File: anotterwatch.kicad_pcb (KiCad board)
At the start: 4 copper layers, 48.5 x 43 mm, 132 parts, among them J1 Micro_SD_Card, J2 Shitty Add-On, J3 Conn_01x05, J4 USB_C_Receptacle_USB2.0, Q1 AO3400, Q2 AO3400, Q3 AO3400, Q4 AO3400, Q5 AO3400, Q6 AO3400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

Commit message: Finished layout
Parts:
- removed C24: 100p, Capacitor_SMD:C_0402_1005Metric
- removed R47: 390k, Resistor_SMD:R_0402_1005Metric
- added C37: 470p, Capacitor_SMD:C_0402_1005Metric, B.Cu at (92.2, 75.7)
- added R50: 10, Resistor_SMD:R_0603_1608Metric, B.Cu at (105.3, 89.5)
- LS1: footprint Connector_Molex:Molex_KK-254_AE-6410-02A_1x02_P2.54mm_Vertical -> Resistor_SMD:R_2816_7142Metric; moved to B.Cu
- moved Q6 85.7 mm to (93.9, 87.8)
- moved LS1 76.6 mm to (100.3, 85.9), turned to 220 degrees
- moved C9 46.9 mm to (87.2, 83.3), turned to 90 degrees
- moved C10 41.2 mm to (91.9, 87.8), turned to 90 degrees
- moved C29 34.6 mm to (96.8, 99.2), turned to 270 degrees
- moved C15 34.1 mm to (104.1, 87.5), turned to 90 degrees
- moved R24 34.0 mm to (103.0, 87.9), turned to 270 degrees
- moved D3 31.2 mm to (86.5, 109.0)
- moved D4 31.2 mm to (118.0, 109.0)
- moved C26 27.3 mm to (80.2, 81.4)
- moved C11 20.2 mm to (112.1, 92.0), turned to 90 degrees
- moved C16 16.7 mm to (114.7, 107.3), turned to 180 degrees
- moved C3 14.5 mm to (89.1, 78.9), turned to 90 degrees
- moved C4 8.43 mm to (106.0, 76.8)
- moved R18 7.41 mm to (106.5, 85.5)
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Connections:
- D5 pad K: (no net) -> +BATT
- J2 pad 1: I2C_SDA -> +3V3
- J2 pad 2: +3V3 -> I2C_SDA
- J2 pad 3: I2C_SCL -> GND
- J2 pad 4: GND -> I2C_SCL
- J4 pad S1: Net-(C24-Pad2) -> GND
- SW1 pad : (no net) -> GND
- U1 pad 12: (no net) -> GND
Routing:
- net Net-(C31-Pad1): track 0.00 -> 116.9 mm, vias 0 -> 5
- net I2C_SDA: track 3.64 -> 76.1 mm, vias 0 -> 6
- net I2C_SCL: track 4.53 -> 67.9 mm, vias 0 -> 5
- net VBUS: track 7.18 -> 58.5 mm, vias 0 -> 8
- net +3V3: track 25.8 -> 70.3 mm, vias 2 -> 27
- net Net-(D2-Pad1): track 0.00 -> 42.0 mm, vias 0 -> 2
- net Net-(D1-Pad1): track 0.00 -> 37.9 mm, vias 0 -> 2
- net BTN_DOWN: track 0.00 -> 34.7 mm, vias 0 -> 3
- net BTN_UP: track 4.80 -> 38.5 mm, vias 0 -> 2
- net BTN_CNTR: track 0.00 -> 33.5 mm, vias 0 -> 3
- net ADC_REF: track 8.34 -> 41.3 mm, vias 0 -> 2
- net Net-(D3-Pad1): track 0.00 -> 31.7 mm, vias 0 -> 2
- net IO0: track 9.60 -> 38.8 mm
- net TXD: track 0.00 -> 28.2 mm, vias 0 -> 2
- net RXD: track 0.00 -> 28.1 mm, vias 0 -> 2
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- added copper zone on In2.Cu, net +3V3
- added copper zone on F.Cu, net GND
- added copper zone on In2.Cu, net GNDA
- removed copper zone on B.Cu, net VBUS

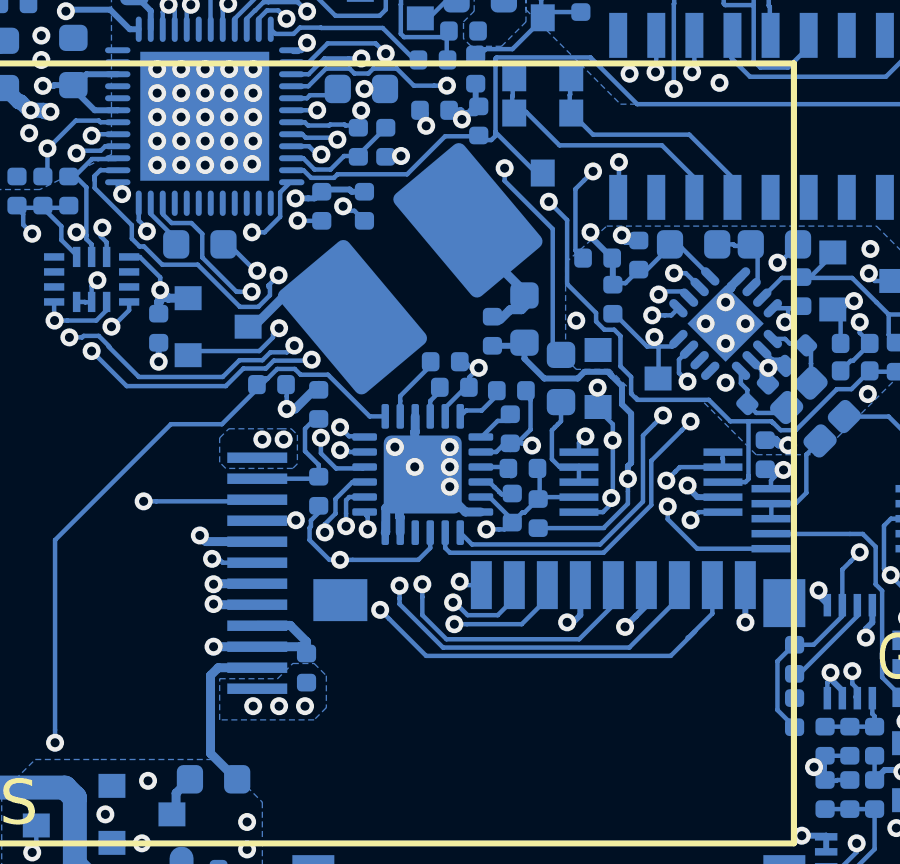
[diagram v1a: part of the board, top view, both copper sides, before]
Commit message: Finished silkscreen
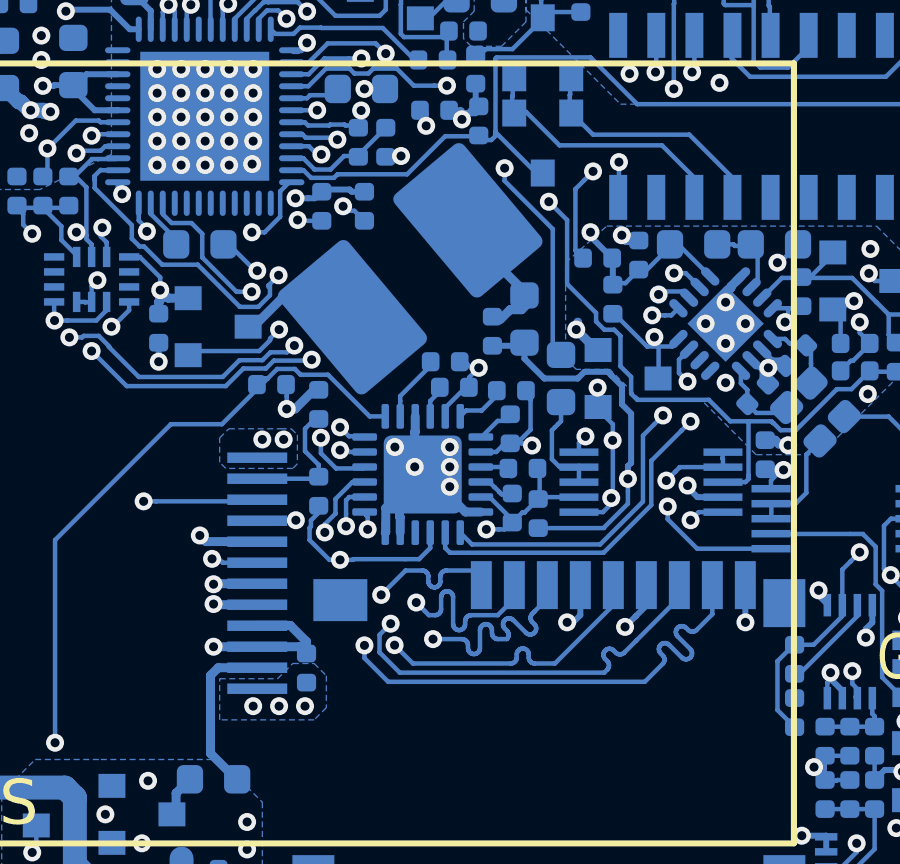
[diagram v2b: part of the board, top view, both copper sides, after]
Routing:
- net ADC_SCK: track 27.9 -> 33.2 mm
- net SD_DATA2: track 31.0 -> 36.1 mm
- net SD_CMD: track 32.1 -> 36.9 mm
- net SD_DATA3: track 32.8 -> 37.5 mm
- net ADC_MISO: track 24.4 -> 29.0 mm
- net SD_DATA1: track 32.4 -> 35.5 mm
- net Net-(J1-Pad7): track 34.0 -> 36.0 mm
- net GND: track 53.2 -> 54.4 mm
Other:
- board text added: "SPEAKER"

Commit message: Final design for first prototype
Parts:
- moved R8 0.05 mm to (97.3, 83.8)
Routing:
- net Net-(AE1-Pad1): track 2.43 -> 4.97 mm
- net Net-(C6-Pad1): track 2.54 -> 4.10 mm
- net GND: vias 129 -> 127

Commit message: ADD: finalized artwork, first pcbs ordered
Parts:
- added G***: LOGO, badgelib:AnOtterWatch_SilkScreen, F.Cu at (103.3, 90.1)
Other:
- board text removed: "-"
- board text removed: "A B GND C CH1 CH2"
- board text removed: "IPS"
- board text removed: "Scope 60V!"
- board text removed: "Tester 3.3V!"

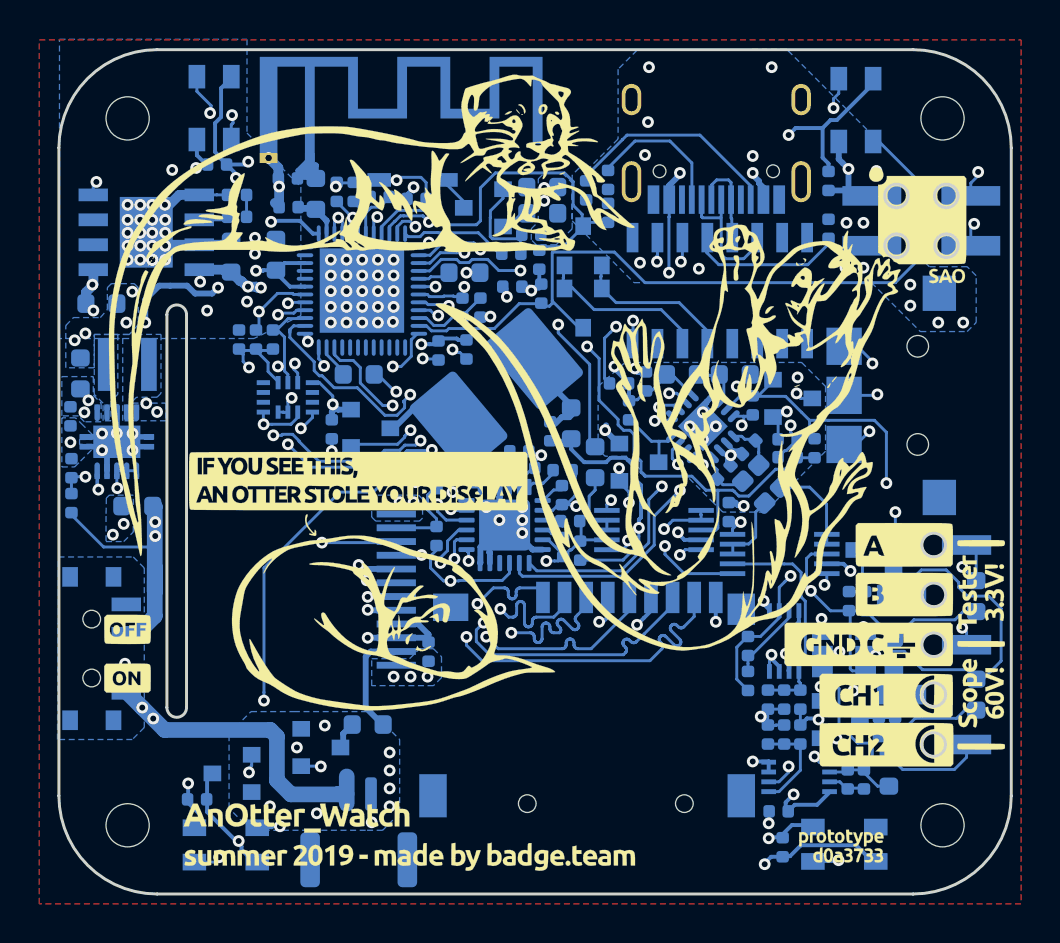
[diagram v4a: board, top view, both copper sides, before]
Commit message: FIX: ESP32 new footprint, fix LED polarity, fix IPS FFC position
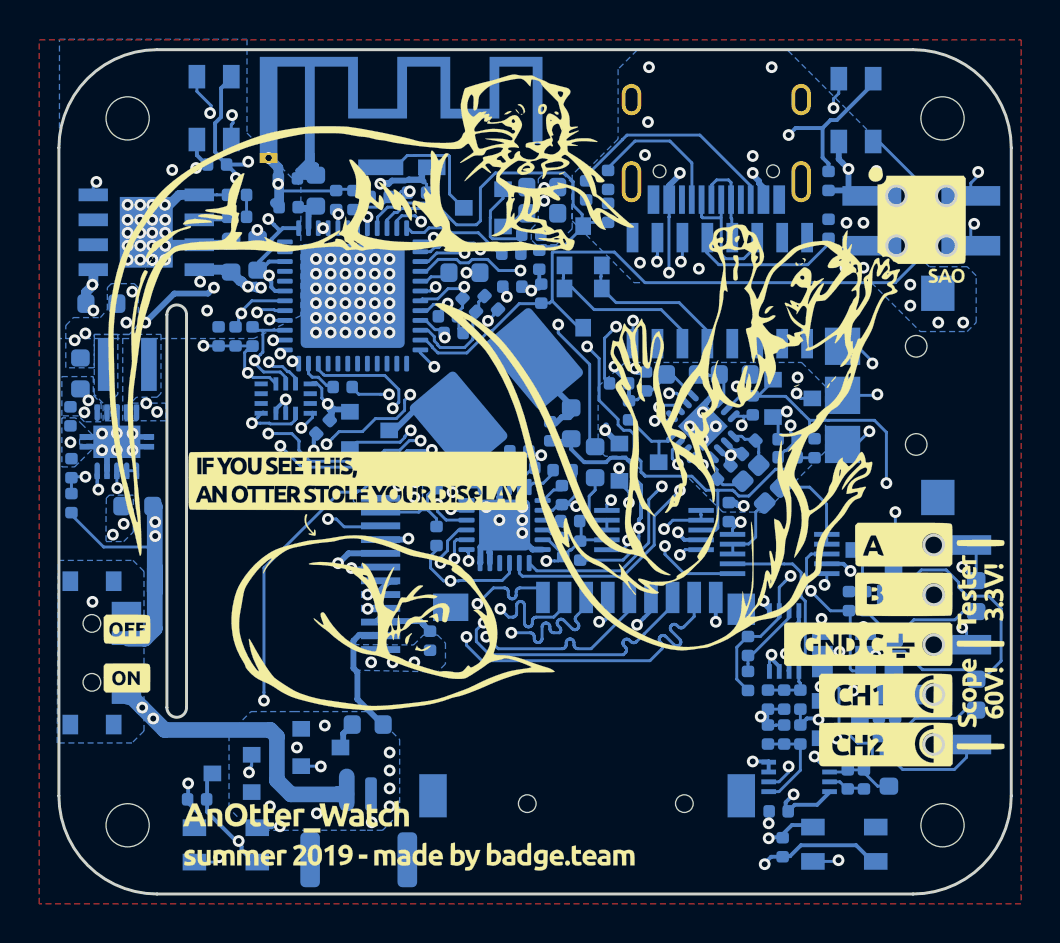
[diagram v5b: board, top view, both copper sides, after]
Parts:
- BT1: footprint badgelib:JST_GH_BM02B-GHS-TBT_1x02-1MP_P1.25mm_Vertical -> Connector_JST:JST_GH_BM02B-GHS-TBT_1x02-1MP_P1.25mm_Vertical
- C6: value TBD -> 4p7
- C7: value TBD -> 3p9
- D5: footprint badgelib:RZX-S020CCW-0.4T -> badgelib:A150GKCBBUP5A
- J1: footprint badgelib:SUNTECH_ST-TF-003A -> ST-TF-003A:SUNTECH_ST-TF-003A
- L1: value TBD -> 1n8
- R13: footprint Resistor_SMD:R_0603_1608Metric -> Resistor_SMD:R_0402_1005Metric
- R16: value 5k1 -> 47k
- U3: footprint ESP32-footprints-Lib:ESP32 -> Package_DFN_QFN:QFN-48-1EP_7x7mm_P0.5mm_EP5.3x5.3mm
- moved R6 1.94 mm to (97.8, 82.1), turned to 180 degrees
- moved R8 1.18 mm to (98.1, 82.9), turned to 180 degrees
- moved U1 1.13 mm to (94.2, 95.2)
- moved R20 1.05 mm to (87.0, 83.1)
- moved R21 1.05 mm to (87.9, 83.1)
- moved C9 1.05 mm to (86.1, 83.1)
- moved R13 1.04 mm to (92.5, 85.7)
- moved C3 0.93 mm to (88.1, 78.9)
- moved D5 0.75 mm to (95.5, 74.6), turned to 180 degrees
- moved R10 0.61 mm to (100.0, 81.4), turned to 135 degrees
- moved U3 0.57 mm to (93.0, 81.0)
- moved C29 0.57 mm to (96.9, 98.6)
- moved C10 0.46 mm to (91.5, 87.7), turned to 45 degrees
- moved C37 0.42 mm to (92.1, 76.2), turned to 90 degrees
- moved C8 0.42 mm to (93.0, 76.2)
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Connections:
- C37 pad 1: GND -> ESP_ADC
- C37 pad 2: ESP_ADC -> GND
- R50 pad 2: ESP_ADC -> Net-(R50-Pad2)
- U7 pad 8: ESP_ADC -> Net-(R50-Pad2)
- U7 pad 9: ESP_ADC -> Net-(R50-Pad2)
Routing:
- net Net-(D5-Pad1): track 1.89 -> 7.25 mm
- net ADC_MISO: track 29.0 -> 33.1 mm, vias 2 -> 4
- net GND: track 54.4 -> 58.4 mm, vias 127 -> 135
- net ESP_ADC: track 27.1 -> 23.2 mm
- net Net-(R50-Pad2): track 0.00 -> 3.56 mm
- net SD_DATA0: track 3.91 -> 6.19 mm
- net VBUS: track 58.5 -> 56.3 mm
- net RXD: track 28.1 -> 30.2 mm
- net I2C_SCL: track 67.7 -> 69.4 mm
- net Net-(R2-Pad2): track 5.48 -> 7.01 mm
- net SD_CMD: track 36.9 -> 35.4 mm, vias 3 -> 2
- net ADC_CS: track 19.1 -> 20.4 mm
- net ADC_SCK: track 33.2 -> 32.0 mm
- net SD_DATA1: track 35.5 -> 36.5 mm
- net BTN_UP: track 38.5 -> 37.6 mm
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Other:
- outline, holes or cut-outs redrawn

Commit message: V1.1 -> Production
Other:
- board text added: "@JLCPCB Please place PCB Reference above this line"
- board text added: "PLACE PCB ID HERE"
- board text added: "prototype V1.1 commit 5b207be"
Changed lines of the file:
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@@
   (general
     (thickness 1.6)
-    (drawings 34)
+    (drawings 41)
     (tracks 2753)
     (zones 0)
@@
       (drillshape 0)
       (scaleselection 1)
-      (outputdirectory "gerber_V1.0"))
+      (outputdirectory "gerber_V1.1"))
   )
   (net 0 "")
@@
     (pad 1 np_thru_hole circle (at 0 0) (size 2.2 2.2) (drill 2.2) (layers *.Cu *.Mask))
   )
+  (gr_text "@JLCPCB\nPlease place PCB \nReference above this line" (at 66 86) (layer F.SilkS)
+    (effects (font (size 1.5 1.5) (thickness 0.3)) (justify right))
+  )
+  (gr_line (start 75.5 86) (end 73.5 88) (layer F.SilkS) (width 0.2))
+  (gr_line (start 75.5 86) (end 73.5 84) (layer F.SilkS) (width 0.2))
+  (gr_line (start 65.5 86) (end 75.5 86) (layer F.SilkS) (width 0.2))
+  (gr_text "PLACE PCB ID HERE" (at 93 88) (layer F.SilkS)
+    (effects (font (size 1 1) (thickness 0.25)))
+  )
+  (gr_line (start 85.5 87) (end 100.5 87) (layer F.SilkS) (width 0.2))
+  (gr_text "prototype V1.1\ncommit 5b207be" (at 114.25 109.6) (layer F.SilkS)
+    (effects (font (size 0.6 0.6) (thickness 0.15)))
+  )
   (gr_text SPEAKER (at 100.33 85.9028 310) (layer B.SilkS)
